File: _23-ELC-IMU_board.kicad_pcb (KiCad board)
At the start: 2 copper layers, 51 x 51.5 mm, 71 parts, among them J1 MX150, J2 MX150, J3 Conn_01x03, J4 Conn_01x02, J5 SWD, SW1 SW_SPDT, U1 LSM6DSR, U2 STM32F105RCTx, U3 SN65HVD230, U4 CD143A-SR05, U5 TPS562200, U6 AMS1117-3.3, Y1 16MHz

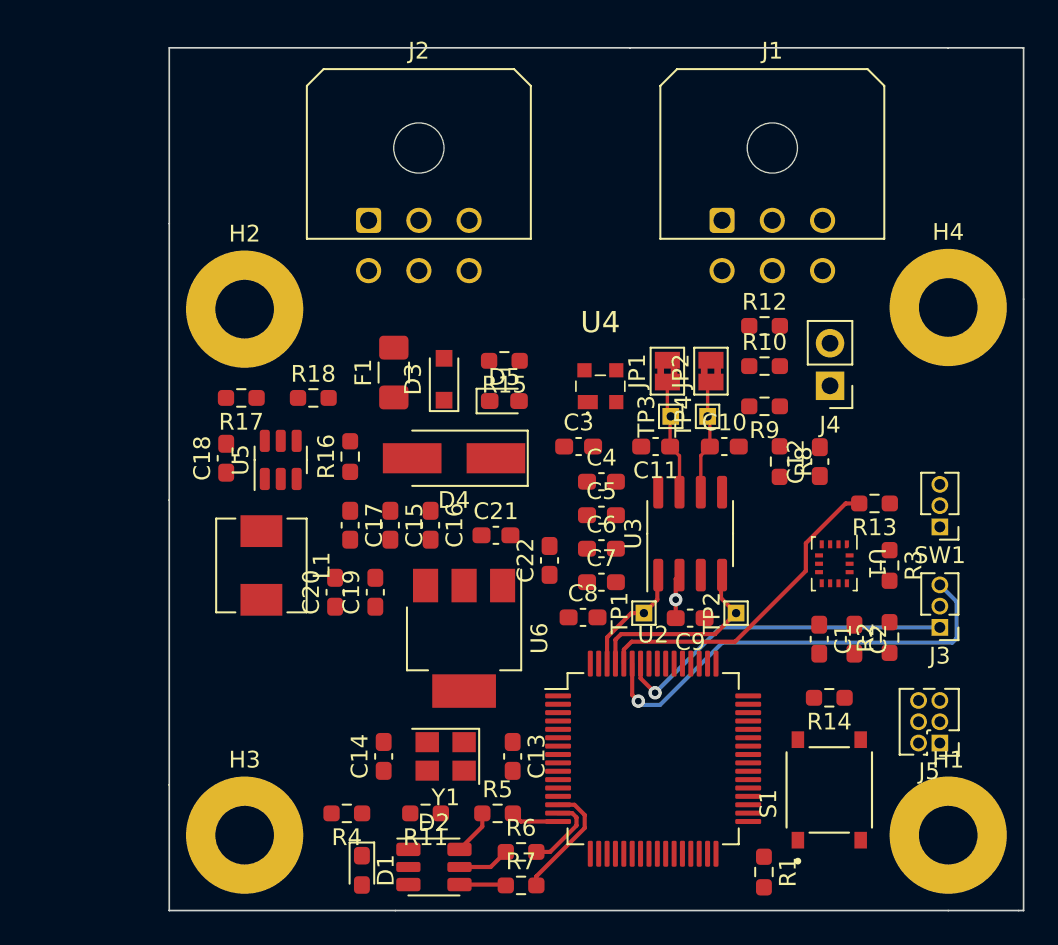
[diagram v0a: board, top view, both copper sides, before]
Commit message: Started drawing like 496130 areas
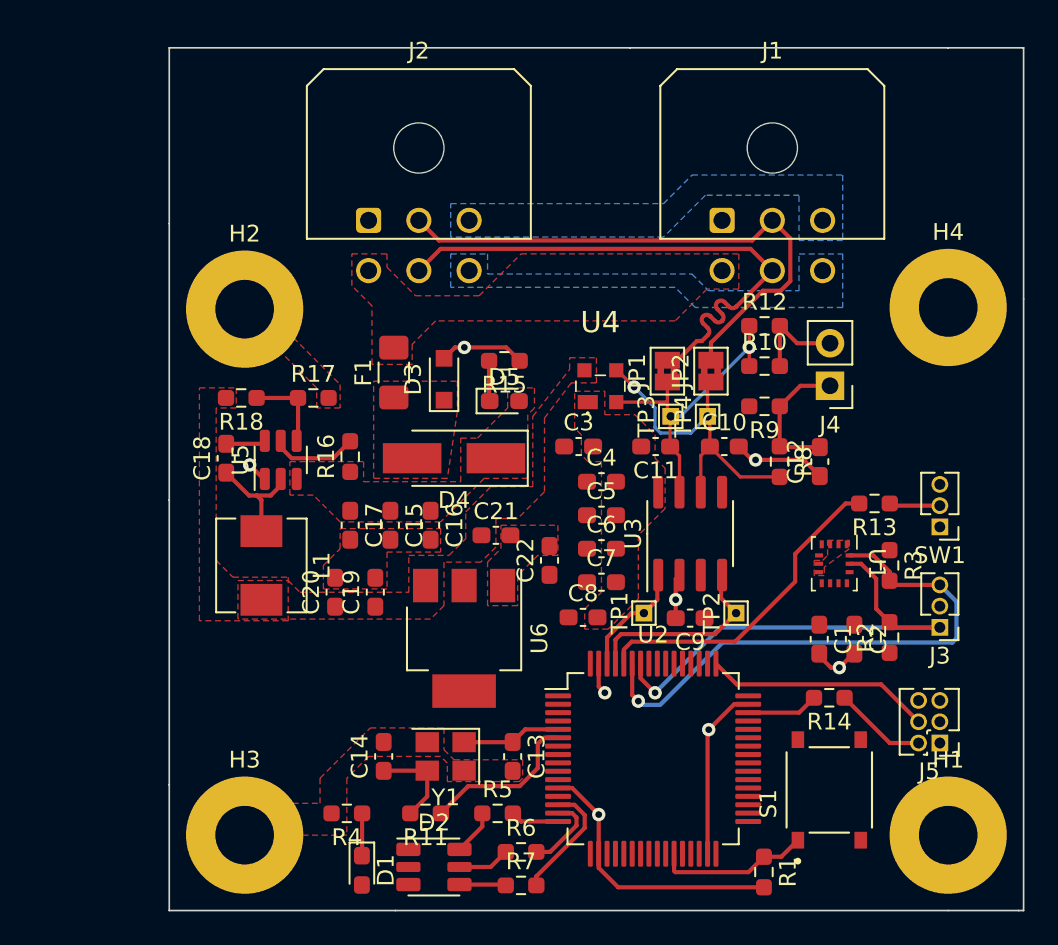
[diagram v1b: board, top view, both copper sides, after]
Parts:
- moved R17 4.30 mm to (75.6, 93.4), turned to 0 degrees
- moved R18 4.30 mm to (71.3, 93.4), turned to 180 degrees
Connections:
- net /CANH renamed /CAN+
- net /CANL renamed /CAN-
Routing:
- net GND: track 2.66 -> 46.4 mm, vias 1 -> 8
- net /CAN+: track 0.00 -> 33.5 mm
- net /CAN-: track 0.00 -> 33.5 mm
- net /Microcontroller/SWCLK: track 0.00 -> 13.5 mm
- net /Microcontroller/DIFF-: track 6.94 -> 20.0 mm, vias 0 -> 1
- net /Microcontroller/DIFF+: track 6.91 -> 18.8 mm, vias 0 -> 1
- net /Microcontroller/HSE_out: track 0.00 -> 9.71 mm
- net /CALIB_BUTTON: track 0.00 -> 9.24 mm
- net Net-(C12-Pad2): track 0.00 -> 8.32 mm
- net /SCL: track 20.7 -> 28.7 mm
- net /VRMS/BUCK/SW: track 0.00 -> 6.69 mm
- net /SDA: track 26.7 -> 33.2 mm
- net /Microcontroller/HSE_in: track 0.00 -> 5.93 mm
- net Net-(J4-Pad2): track 0.00 -> 5.83 mm
- net Net-(C14-Pad1): track 0.00 -> 5.57 mm
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- added copper zone on F.Cu, net +24V
- added copper zone on F.Cu, net +5V
- added copper zone on B.Cu, net /P3
- added copper zone on F.Cu, net /VRMS/BUCK/V_in
- added copper zone on F.Cu, net /VRMS/DIODE
- added copper zone on F.Cu, net GND
- added copper zone on B.Cu, net Net-(J1-Pad6)

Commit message: All pours done
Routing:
- net +3V3: track 0.00 -> 55.3 mm
- net GND: track 46.4 -> 89.3 mm, vias 8 -> 15
- net +5V: track 0.00 -> 4.24 mm
- net /Microcontroller/DIFF-: track 20.0 -> 22.1 mm
- net /VRMS/DIODE: track 0.76 -> 0.00 mm
- net /CAN+: track 33.5 -> 32.9 mm
- added copper zone on F.Cu, net +3V3
- added copper zone on B.Cu, net GND
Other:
- outline, holes or cut-outs redrawn

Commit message: I am happy with this layout
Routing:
- net +5V: track 4.24 -> 0.00 mm

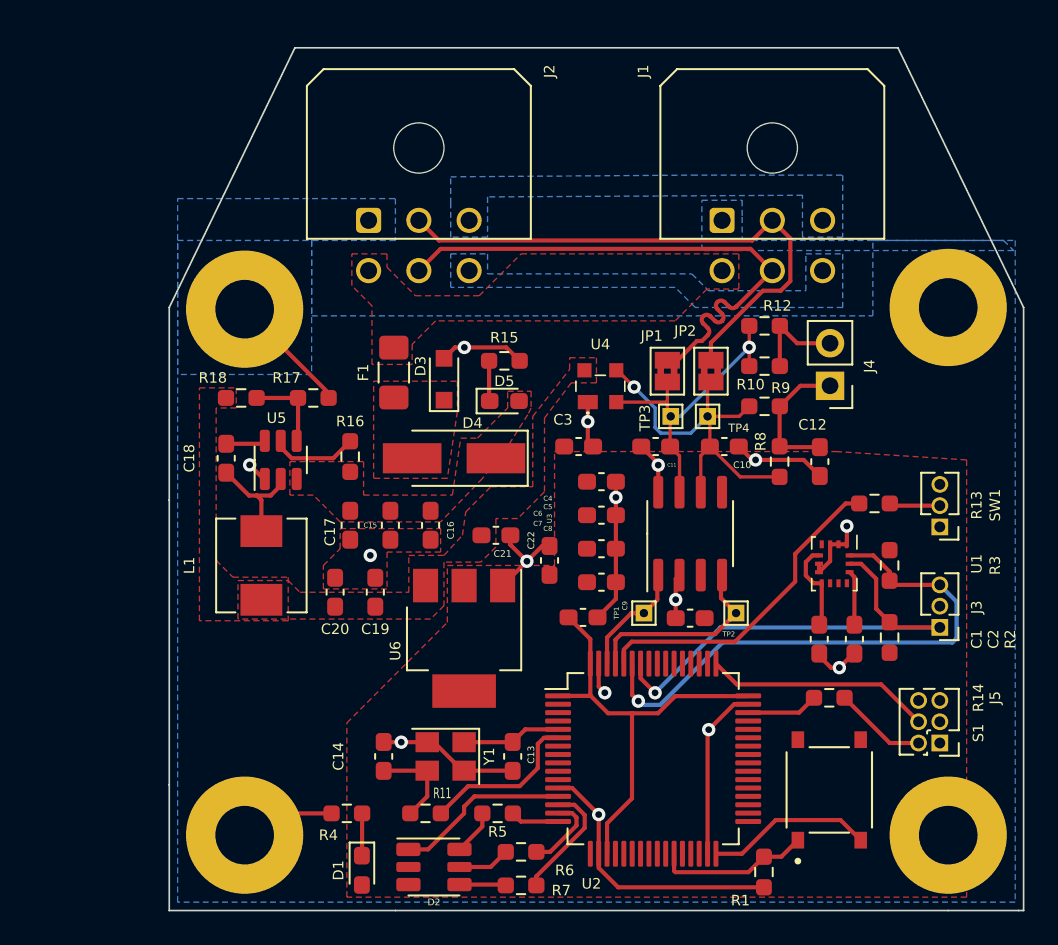
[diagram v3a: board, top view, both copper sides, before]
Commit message: Added 0 Ohm resistor between shield (grounded)
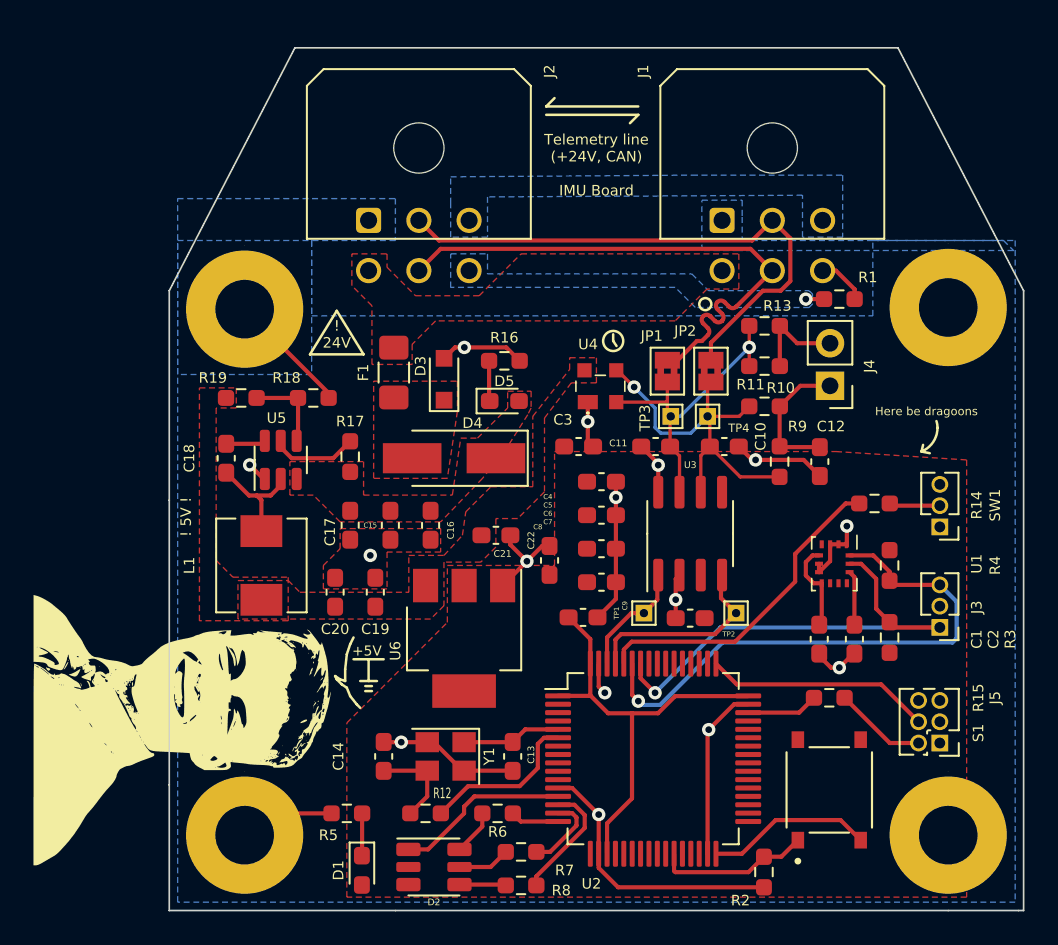
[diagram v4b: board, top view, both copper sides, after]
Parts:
- added G***: LOGO, Global Libraries:rylan, F.Cu at (68.9, 111.3)
- added R1: 0 Ohm, Resistor_SMD:R_0603_1608Metric_Pad0.98x0.95mm_HandSolder, F.Cu at (107.0, 87.5)
- renumbered R9 to R10, R10 to R11, R11 to R12, R12 to R13, R13 to R14, R14 to R15, R15 to R16, R16 to R17, R17 to R18, R18 to R19, R1 to R2, R2 to R3, R3 to R4, R4 to R5, R5 to R6, R6 to R7, R7 to R8, R8 to R9
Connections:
- J1 pad 6: Net-(J1-Pad6) -> GND
- J2 pad 6: Net-(J1-Pad6) -> GND
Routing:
- net GND: track 89.3 -> 93.3 mm, vias 15 -> 16
- removed copper zone on B.Cu, net Net-(J1-Pad6)
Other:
- outline, holes or cut-outs redrawn
- board text added: "! 24V"
- board text added: "! 5V !"
- board text added: "+5V"
- board text added: "Here be dragoons"
- board text added: "Telemetry line (+24V, CAN) IMU Board"

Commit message: Connected final things for this iteration of the board
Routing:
- net GND: track 93.3 -> 99.1 mm
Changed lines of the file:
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@@
   (segment (start 72.6375 98.2375) (end 71.8 97.4) (width 0.25) (layer "F.Cu") (net 2))
   (segment (start 76.5125 93.1125) (end 71.5 88.1) (width 0.25) (layer "F.Cu") (net 2))
+  (segment (start 107.9125 87.5) (end 108.4125 88) (width 0.25) (layer "F.Cu") (net 2))
   (segment (start 101.7975 97.1) (end 100.9975 96.3) (width 0.25) (layer "F.Cu") (net 2))
   (segment (start 107.45 102.1375) (end 106.95 102.1375) (width 0.25) (layer "F.Cu") (net 2))
@@
   (segment (start 92.635 109.26) (end 92.635 110.635) (width 0.25) (layer "F.Cu") (net 2))
   (segment (start 90.21 116.685) (end 91.050685 116.685) (width 0.25) (layer "F.Cu") (net 2))
+  (segment (start 108.4125 88) (end 113.5 88) (width 0.25) (layer "F.Cu") (net 2))
   (segment (start 84.055 90.385) (end 83.405 91.035) (width 0.25) (layer "F.Cu") (net 2))
   (segment (start 93.6625 102.4) (end 93.6625 100.4) (width 0.25) (layer "F.Cu") (net 2))
@@
         (xy 74.2 97.2)
         (xy 78.6 97.2)
-        (xy 78.6 99.2)
-        (xy 83.9 99.2)
+        (xy 78.6 98.7)
+        (xy 83.9 98.7)
         (xy 84.4 95.8)
         (xy 85.4 95.8)
@@
         (xy 105.4 87.2)
         (xy 105.4 87.8)
-        (xy 105.2 88)
-        (xy 98.4 88)
+        (xy 105.4 88.7)
+        (xy 98.9 88.7)
         (xy 97.2 86.8)
         (xy 83.8 86.8)
